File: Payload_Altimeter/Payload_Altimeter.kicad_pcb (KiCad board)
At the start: 2 copper layers, 80 x 93.3 mm, 5 parts, among them J1 L717SDC37P1ACH4F, J2 Conn_01x09, U1 Arduino_Pro_Mini, U7 MS5607-02BA

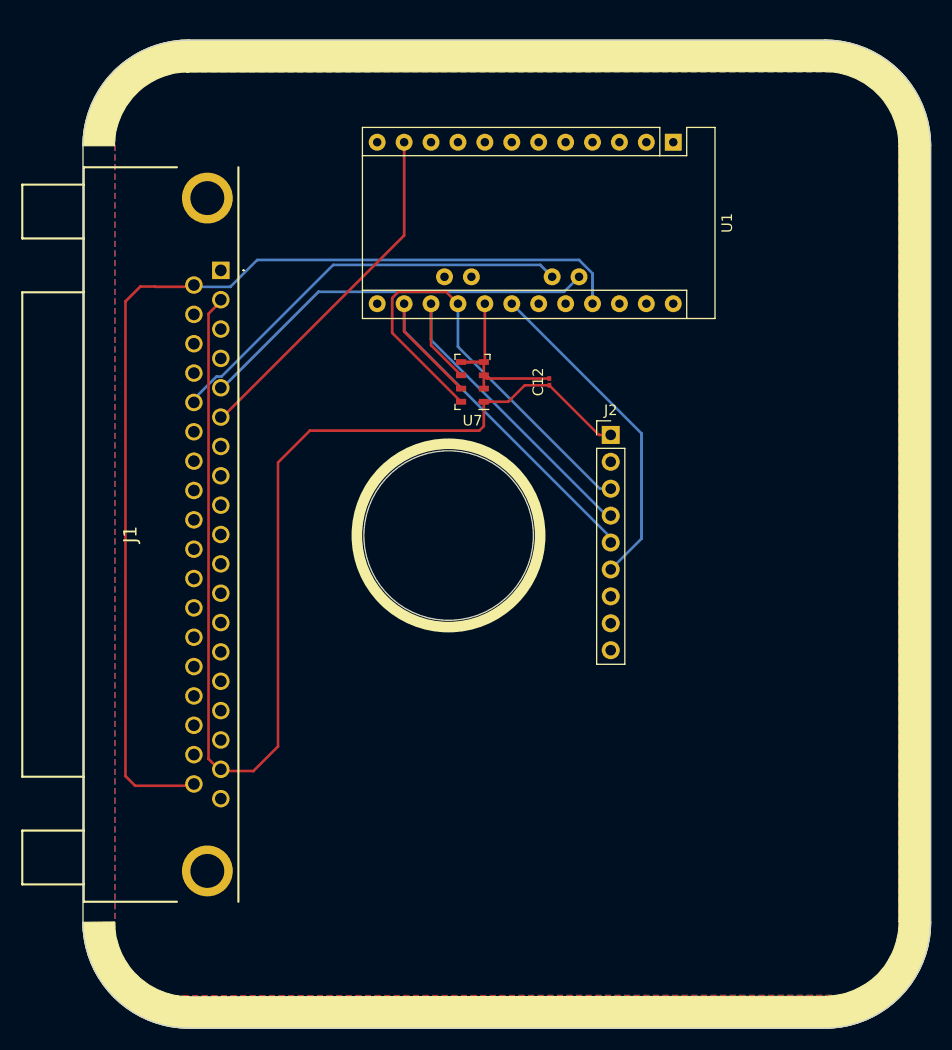
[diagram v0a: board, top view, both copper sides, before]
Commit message: Corrected edge cuts, aligned center hole, adjusted silkscreen border, aligned grid, aligned all components
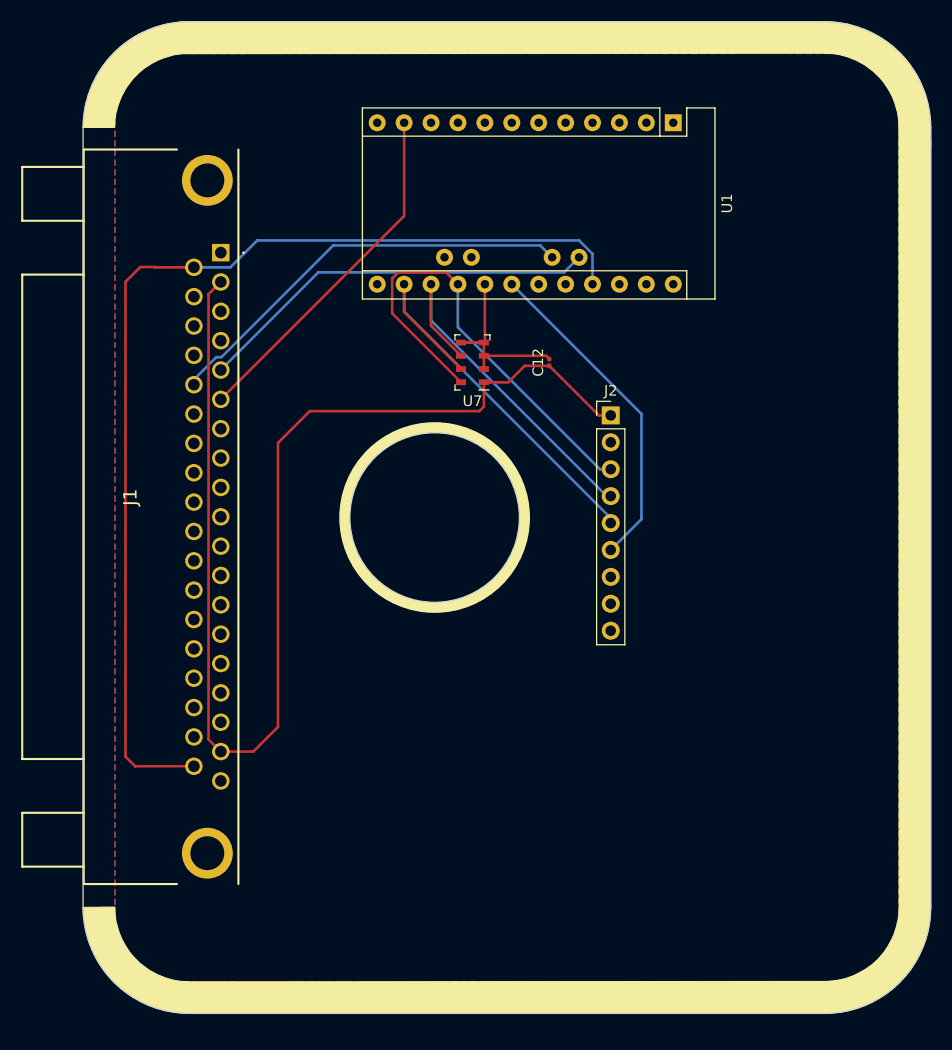
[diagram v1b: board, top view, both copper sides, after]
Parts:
- added G***: LOGO, RDT_Graphics:RDT_Logo, B.Cu at (100.6, 96.8)
- moved U1 1.84 mm to (135.7, 59.5)
- moved C12 1.84 mm to (124.0, 82.2)
- moved J2 1.84 mm to (129.8, 87.2)
- moved U7 1.84 mm to (116.8, 82.2)
- moved J1 1.67 mm to (93.0, 71.8)
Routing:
- net /Altimeter/~{CSB}: track 12.3 -> 11.1 mm
- net GND: track 6.30 -> 7.55 mm
- net +3V3: track 117.7 -> 116.7 mm
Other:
- board size 80 x 93.3 mm -> 80 x 93.6 mm

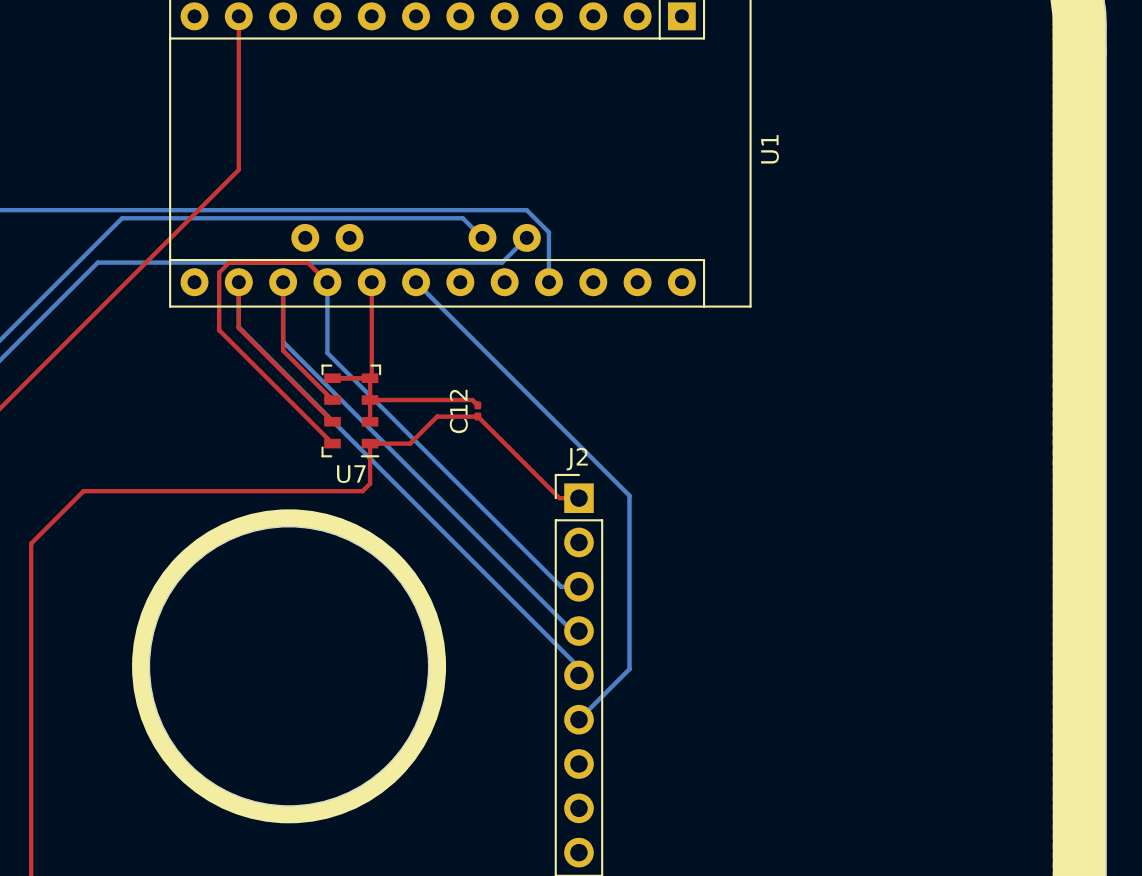
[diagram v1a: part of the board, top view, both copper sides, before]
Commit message: Adjusted silkscreen
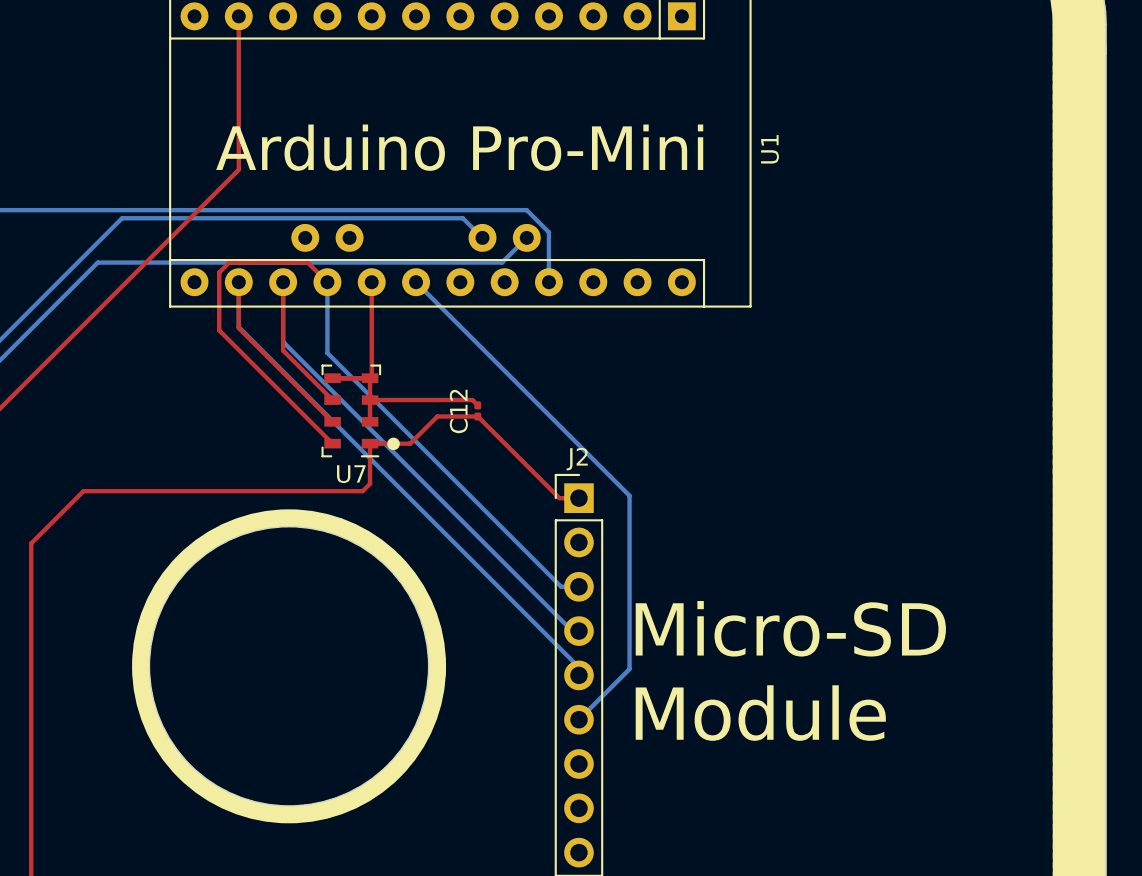
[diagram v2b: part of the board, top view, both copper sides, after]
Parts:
- added G***: LOGO, Graphics:Orientation_Marker, B.Cu at (92.4, 57.5)
- added G***: LOGO, Graphics:Orientation_Marker, B.Cu at (92.4, 136.0)
- added G***: LOGO, Graphics:Isaac_Signature, B.Cu at (120.0, 135.0)
- added G***: LOGO, Graphics:Payload_QR_Code, B.Cu at (145.0, 96.8)
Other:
- board text added: "Arduino Pro-Mini"
- board text added: "Isaac Washburn"
- board text added: "Micro-SD Module"
- board text added: "Payload Altimeter Module Rev. 1"
- board text added: "THIS END IN"

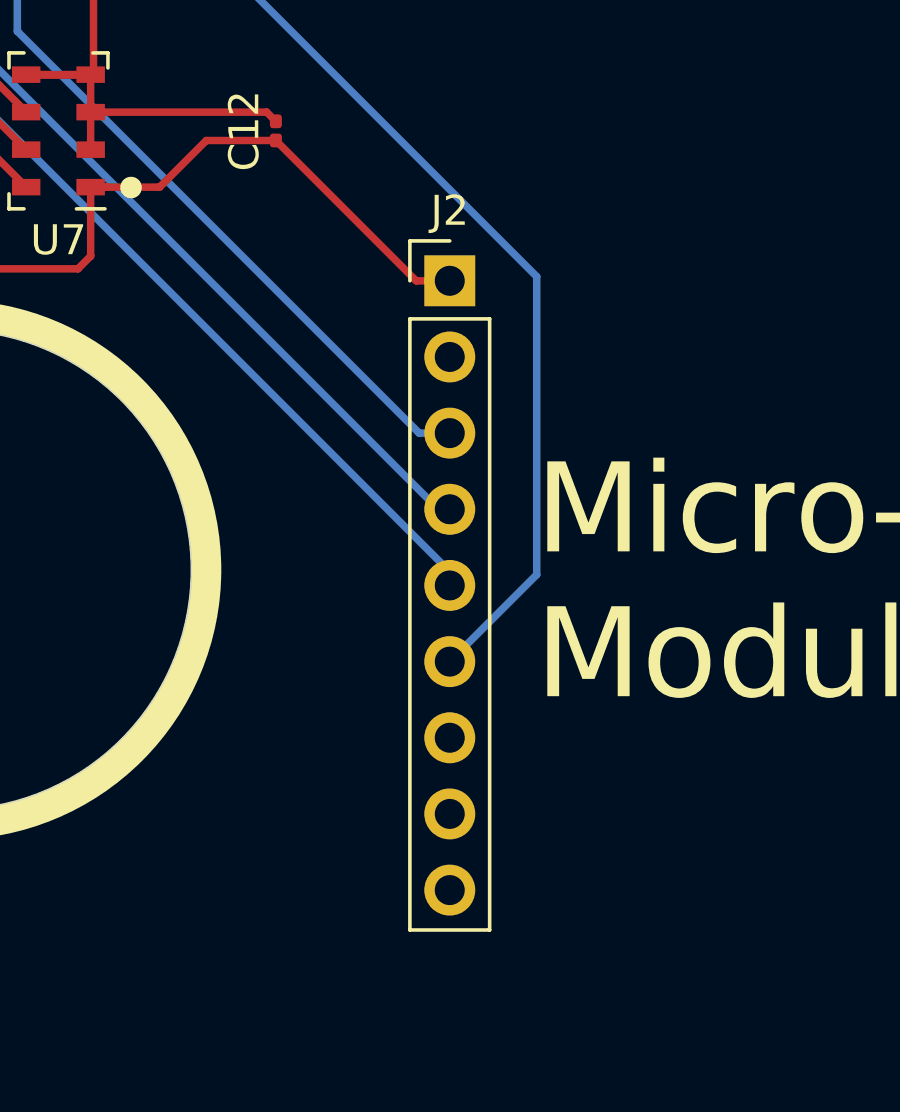
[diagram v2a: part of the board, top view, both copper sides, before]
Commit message: Deleted SD
Got rid of the SD card on the PCB the teensy will now be what is housing the SD card
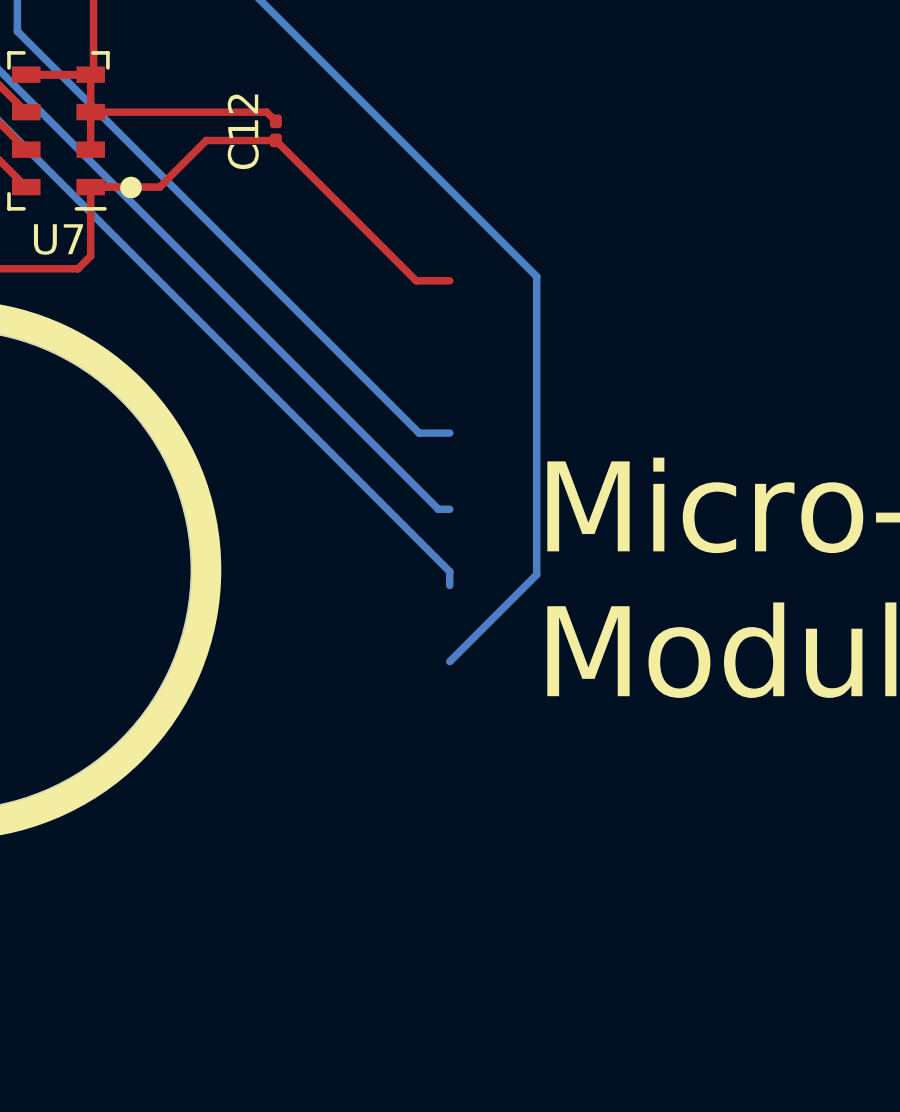
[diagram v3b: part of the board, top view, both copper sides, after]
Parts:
- removed the G*** at (100.6, 96.8)
- removed J2: Conn_01x09, Connector_PinHeader_2.54mm:PinHeader_1x09_P2.54mm_Vertical
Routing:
- net GND: track 7.55 -> 18.6 mm
- net /Altimeter/~{CSB}: track 11.1 -> 0.00 mm

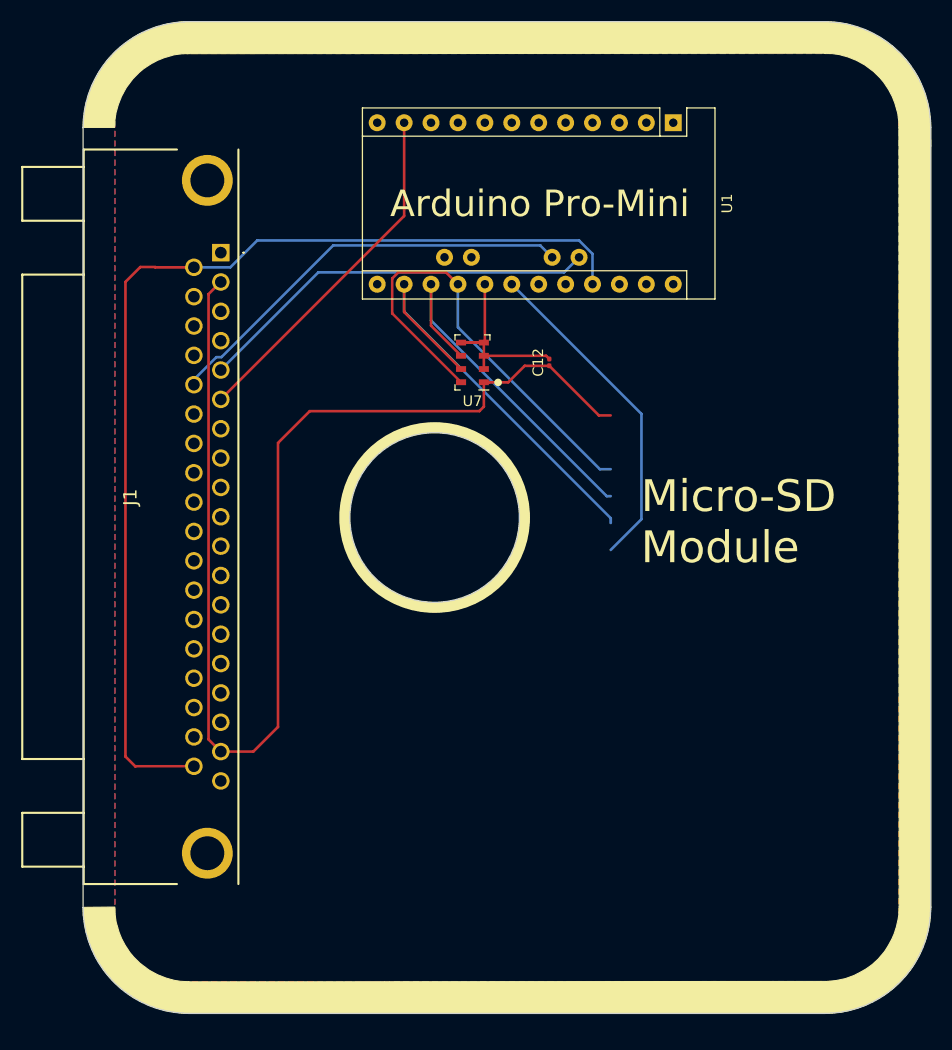
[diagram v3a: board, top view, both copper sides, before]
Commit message: Rasp_Pi
Tried to put in a pi zero
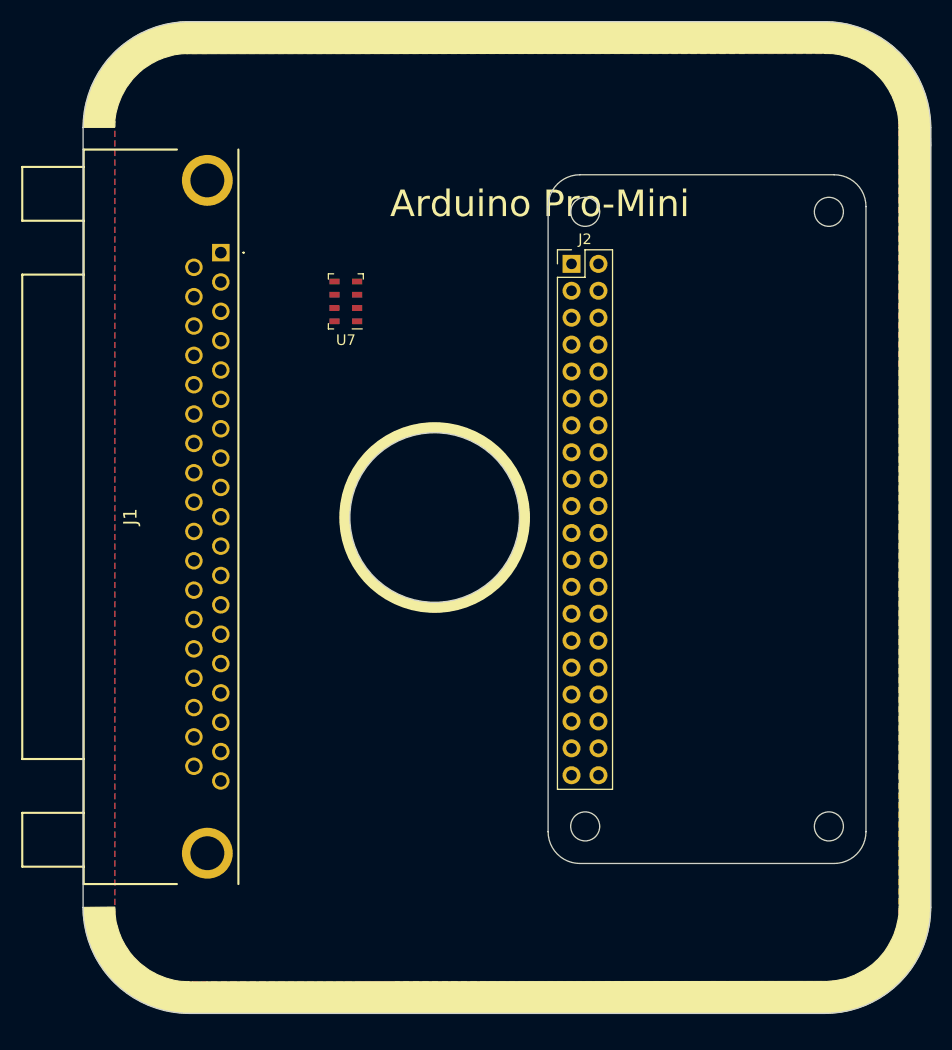
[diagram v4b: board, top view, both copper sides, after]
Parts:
- removed C12: 100nF, Capacitor_SMD:C_0201_0603Metric
- removed the G*** at (145.0, 96.8)
- removed U1: Arduino_Pro_Mini, Arduino:Arduino_Pro_Mini
- added J2: Conn_02x20_Odd_Even, Connector_PinHeader_2.54mm:PinHeader_2x20_P2.54mm_Vertical, F.Cu at (126.1, 72.9)
- moved U7 13.3 mm to (104.8, 76.4)
- moved G*** 0.59 mm to (119.7, 134.5)
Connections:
- J1 pad 24: /Arduino/I2C_SDA -> /DSUB/Alert_sda
- J1 pad 5: /Arduino/I2C_SCL -> /DSUB/Alert_scl
- J1 pad 6: /Arduino/I2C_EN -> /DSUB/Alert_Active
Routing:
- net +3V3: track 116.7 -> 0.00 mm
- net +5V: track 100.7 -> 0.00 mm
- net /Altimeter/SCLK: track 43.4 -> 0.00 mm
- net /Altimeter/SDI_SDA: track 40.8 -> 0.00 mm
- net /Arduino/I2C_SDA: track 40.0 -> 0.00 mm
- net /Arduino/I2C_SCL: track 38.2 -> 0.00 mm
- net /Altimeter/SDO: track 35.2 -> 0.00 mm
- net /Arduino/I2C_EN: track 33.3 -> 0.00 mm
- net /Arduino/sd_cs: track 31.4 -> 0.00 mm
- net GND: track 18.6 -> 0.00 mm
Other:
- outline, holes or cut-outs redrawn
- board text added: "License: MIT - Copyright 2018 StudioPieters®"
- board text added: "PP1"
- board text added: "PP6"
- board text added: "Project name: Raspberry Pi® Zero W - Hat template Project URI: https://www.studiopieters.nl Description: Kicad - Raspberry Pi® Zero W Hat template package Version: 1.0.8"
- board text removed: "Micro-SD Module"
- board text removed: "Payload Altimeter Module Rev. 1"

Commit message: Finished Schematic?
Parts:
- moved J2 48.3 mm to (128.6, 121.1), turned to 180 degrees
